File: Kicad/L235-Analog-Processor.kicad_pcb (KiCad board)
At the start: 2 copper layers, 190 x 125 mm, 295 parts, among them IC2 AD633ARZ-RL, J1 Input A, J10 Half Wave A + -B, J11 Inverted Out B, J12 CV Select, J13 CV Select, J15 Inverted Out A, J16 Full-Wave Rectifier A, J17 Half-Wave Rectifier A, J18 √(A²+B²), J2 Input B, J3 Function IN, J4 ( 10A / |B| ) / ( A * B / 10 ), J5 Output F(x), J6 Power, J7 Full-Wave Rectifier B, J8 A - B, J9 Negative Half-Wave Rectifier B, U1 TL082, U10 TL082, U11 TL082, U12 TL082, U13 TL084, U15 TL082, U16 RC4580, U17 TL082, U18 LM4040DBZ-10, U19 74HC148, U2 TL082, U20 LM339, U21 LM339, U22 74LS151, U23 74LS151, U24 74LS151, U25 74LS151, U26 74LS151, U27 74LS151, U28 74LS151, U29 LM339, U3 TL082, U30 LM339, U31 74HC148, U32 74LS151, U33 74LS151, U34 74LS151, U35 74LS151, U36 LM78M05_TO252, U4 TL082, U5 TL082, U6 TL082, U7 TL082, U8 TL082, U9 TL082

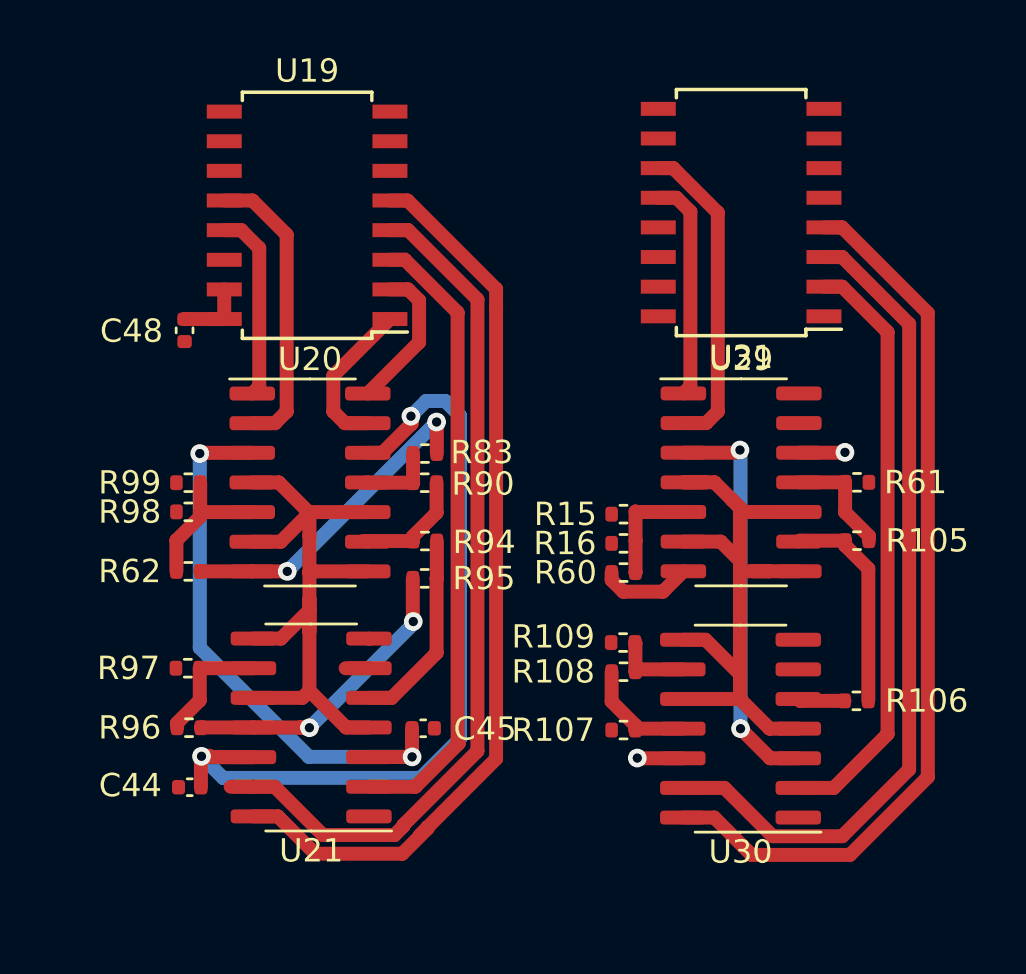
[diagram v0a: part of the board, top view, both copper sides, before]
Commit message: Added example of 3-bit flash adc and explained choice AD633
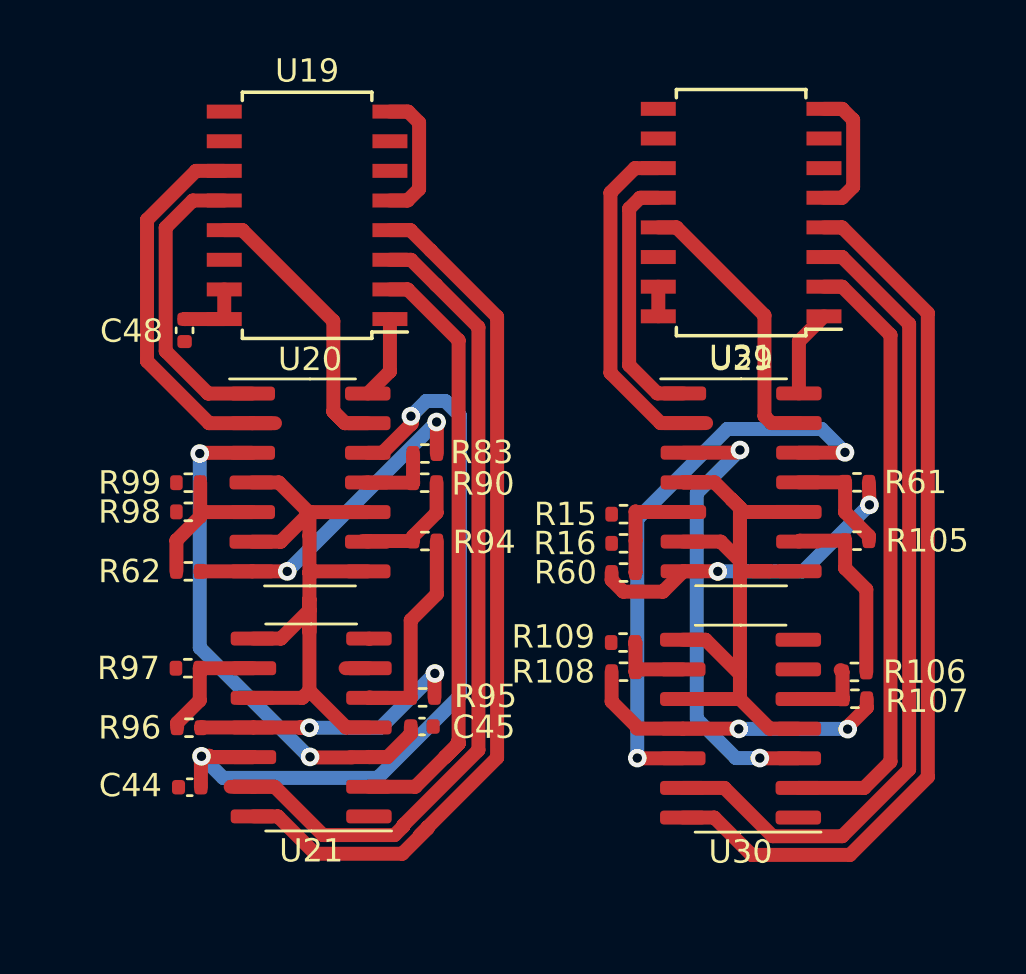
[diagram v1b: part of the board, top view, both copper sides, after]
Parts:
- moved R107 10.0 mm to (436.9, 3.66)
- moved R95 5.10 mm to (418.4, 3.60), turned to 180 degrees
- moved R106 1.24 mm to (436.9, 2.51)
- moved C45 0.09 mm to (418.4, 4.85)
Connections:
- U19 pad 1: Net-(U19-I4) -> Net-(U19-4)
- U19 pad 10: GND -> unconnected-(U19-0-Pad10)
- U19 pad 11: unconnected-(U19-I1-Pad11) -> Net-(U19-1)
- U19 pad 12: Net-(U19-I2) -> Net-(U19-2)
- U19 pad 13: Net-(U19-I3) -> Net-(U19-3)
- U19 pad 2: Net-(U19-I5) -> Net-(U19-5)
- U19 pad 3: Net-(U19-I6) -> Net-(U19-6)
- U19 pad 4: Net-(U19-I7) -> Net-(U19-7)
- U19 pad 5: Net-(U19-EI) -> GND
- U20 pad 1: Net-(U19-I3) -> Net-(U19-2)
- U20 pad 13: Net-(U19-I4) -> Net-(U19-3)
- U20 pad 14: Net-(U19-I5) -> Net-(U19-4)
- U20 pad 2: Net-(U19-I2) -> Net-(U19-1)
- U21 pad 13: Net-(U19-I7) -> Net-(U19-6)
- U21 pad 14: Net-(U19-EI) -> Net-(U19-7)
- U21 pad 2: Net-(U19-I6) -> Net-(U19-5)
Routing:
- net Net-(U19-EI): track 39.5 -> 0.00 mm
- net Net-(U19-7): track 0.00 -> 38.3 mm
- net Net-(U19-I7): track 37.3 -> 0.00 mm
- net Net-(U19-6): track 0.00 -> 36.1 mm
- net Net-(U19-I6): track 26.9 -> 0.00 mm
- net Net-(U19-5): track 0.00 -> 26.6 mm
- net -12V: track 105.0 -> 125.1 mm
- net Net-(U19-1): track 0.00 -> 16.8 mm
- net Net-(U19-2): track 0.00 -> 12.7 mm
- net Net-(U19-3): track 0.00 -> 12.6 mm
- net Net-(U19-I2): track 12.5 -> 0.00 mm
- net Net-(U31-3): track 0.00 -> 12.0 mm
- net GND: track 19.1 -> 30.7 mm
- net Net-(U29B-+): track 3.96 -> 14.4 mm, vias 0 -> 2
- net Net-(U30C-+): track 4.98 -> 13.9 mm, vias 0 -> 2
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
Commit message: Added header and mounting points
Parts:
- added ?: , , F.Cu at (374.0, 105.5)
- added H1: MountingHole, MountingHole:MountingHole_3.2mm_M3_DIN965, F.Cu at (374.0, 3.50)
- added H1: MountingHole, MountingHole:MountingHole_3.2mm_M3_DIN965, F.Cu at (319.0, 3.50)
- added H2: MountingHole, MountingHole:MountingHole_3.2mm_M3_DIN965, F.Cu at (393.0, 3.50)
- added H2: MountingHole, MountingHole:MountingHole_3.2mm_M3_DIN965, F.Cu at (338.0, 3.50)
- added H3: MountingHole, MountingHole:MountingHole_3.2mm_M3_DIN965, F.Cu at (319.0, 105.5)
- added H3: MountingHole, MountingHole:MountingHole_3.2mm_M3_DIN965, F.Cu at (374.0, 105.5)
- added J14: Conn_01x12_Pin, Connector_PinHeader_2.54mm:PinHeader_1x18_P2.54mm_Vertical, F.Cu at (338.0, 31.6)
- added J19: Conn_01x12_Socket, Connector_PinHeader_2.54mm:PinHeader_1x18_P2.54mm_Vertical, F.Cu at (393.0, 31.6)
- C10: value 0.01uF -> 10nF; footprint Capacitor_THT:C_Rect_L7.0mm_W2.5mm_P5.00mm -> Capacitor_SMD:C_0402_1005Metric
- C38, C39, D27, D28, RV1, RV2, RV3, RV4, RV5, RV6: moved to B.Cu
- C9: value 0.001uF -> 1nF; footprint Capacitor_THT:C_Rect_L7.0mm_W2.5mm_P5.00mm -> Capacitor_SMD:C_0402_1005Metric
- D24: footprint Diode_SMD:D_0402_1005Metric -> LED_THT:LED_D3.0mm_Clear
- J6: footprint Custom_Footprints:Eurorack_16_pin_header -> Custom_Footprints:Eurorack_10_pin_header; moved to B.Cu
- RV7, RV8: footprint Potentiometer_THT:Potentiometer_Alps_RK163_Single_Horizontal -> Potentiometer_THT:Potentiometer_Alpha_RD901F-40-00D_Single_Vertical
- moved C73 405.7 mm to (406.9, 52.0), turned to 180 degrees
- moved C72 397.9 mm to (398.7, 57.2), turned to -90 degrees
- moved R12 375.7 mm to (389.5, 35.8)
- moved R11 373.5 mm to (387.5, 35.3), turned to -90 degrees
- moved R14 372.9 mm to (386.8, 45.1)
- moved R10 371.3 mm to (385.6, 35.8), turned to 180 degrees
- moved R9 371.2 mm to (385.6, 34.8)
- moved R13 370.7 mm to (384.8, 45.1)
- moved C81 319.5 mm to (375.8, 37.4), turned to -90 degrees
- moved C82 315.7 mm to (374.5, 48.2), turned to 90 degrees
- moved IC2 302.1 mm to (375.2, 43.5), turned to -90 degrees
- moved U16 298.0 mm to (372.5, 34.5), turned to 90 degrees
- moved R59 297.4 mm to (339.2, 107.0), turned to -90 degrees
- moved R73 288.0 mm to (337.5, 102.8), turned to 180 degrees
- moved R70 287.7 mm to (337.5, 89.0)
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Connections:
- R91 pad 2: * OUT -> AD534_OUT
- U22 pad 12: B_IN_BUFFERED -> B
- U22 pad 15: A_IN_BUFFERED -> A
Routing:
- net -12V: track 125.1 -> 456.5 mm, vias 8 -> 24
- net +12V: track 85.7 -> 406.2 mm, vias 7 -> 21
- net +5V: track 4.24 -> 133.6 mm, vias 0 -> 3
- net A: track 127.3 -> 254.5 mm, vias 0 -> 6
- net GND: track 30.7 -> 137.8 mm, vias 11 -> 20
- net <X>: track 0.00 -> 105.7 mm, vias 0 -> 1
- net B0: track 0.00 -> 105.1 mm, vias 0 -> 5
- net Net-(U7B--): track 0.00 -> 96.0 mm
- net A1: track 0.00 -> 79.3 mm, vias 0 -> 5
- net A2: track 0.00 -> 77.0 mm, vias 0 -> 5
- net AD534_OUT: track 0.00 -> 72.3 mm, vias 0 -> 6
- net A0: track 0.00 -> 71.3 mm, vias 0 -> 6
- net B: track 106.0 -> 176.8 mm, vias 0 -> 2
- net B2: track 0.00 -> 54.0 mm, vias 0 -> 4
- net Net-(J18-PadT): track 0.00 -> 53.2 mm, vias 0 -> 1
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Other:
- board size 190 x 125 mm -> 110 x 110 mm
- board text added: "Input A"
- board text added: "Input B"

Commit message: Optimized PCB routing, started with variable resistor
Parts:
- removed ?: , 
- removed U16: RC4580, Package_SO:SOIC-8_3.9x4.9mm_P1.27mm
- added U14: RC4580, Package_SO:SOIC-8_3.9x4.9mm_P1.27mm, F.Cu at (380.8, 35.9)
- added U37: TL082, Package_SO:SOIC-8_3.9x4.9mm_P1.27mm, F.Cu at (404.7, 25.3)
- C25: footprint Capacitor_THT:C_Rect_L7.0mm_W2.5mm_P5.00mm -> Capacitor_SMD:C_0402_1005Metric
- U22, U23, U24, U25, U26, U28, U32, U33, U34, U35: value 74LS151 -> DG4051E
- moved R33 268.2 mm to (411.1, 5.21), turned to 90 degrees
- moved RV3 263.7 mm to (406.3, 3.10), turned to -90 degrees
- moved C70 262.0 mm to (383.9, 80.2), turned to 180 degrees
- moved R27 259.4 mm to (410.5, 26.4), turned to -90 degrees
- moved R22 257.8 mm to (409.5, 14.0), turned to 90 degrees
- moved R31 256.1 mm to (402.3, 11.9)
- moved R23 253.3 mm to (404.5, 11.9), turned to 180 degrees
- moved R25 253.1 mm to (404.5, 21.9)
- moved R26 252.5 mm to (403.4, 20.6)
- moved R28 252.4 mm to (400.2, 8.14), turned to 90 degrees
- moved R29 251.7 mm to (401.0, 20.6), turned to 180 degrees
- moved R30 251.5 mm to (398.8, 13.4)
- moved R32 251.3 mm to (398.9, 23.1)
- moved R24 249.2 mm to (400.5, 16.6), turned to -90 degrees
- moved R21 248.8 mm to (401.1, 32.1)
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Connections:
- C25 pad 1: Net-(U11A--) -> Net-(U37A--)
- J14 pad 16: √(A²+B²) -> GND
- J14 pad 2: A -> X
- J14 pad 4: B -> √(A²+B²)
- J14 pad 6: X -> A
- J14 pad 8: GND -> -12V
- J14 pad 9: -12V -> B
- J15 pad G: GND -> unconnected-(J15-PadG)
- J19 pad 16: √(A²+B²) -> GND
- J19 pad 2: A -> X
- J19 pad 4: B -> √(A²+B²)
- J19 pad 6: X -> A
- J19 pad 8: GND -> -12V
- J19 pad 9: -12V -> B
- R25 pad 1: Net-(U13A-+) -> Net-(U37B--)
- R26 pad 2: Net-(U13A-+) -> Net-(U37B--)
- R27 pad 1: Net-(U11A--) -> Net-(U37A--)
- R30 pad 1: Net-(U13A--) -> Net-(U37B-+)
- R33 pad 2: Net-(U6A-+) -> Net-(R33-Pad2)
- RV3 pad 1: Net-(U6A-+) -> Net-(R33-Pad2)
- TR1 pad 4: Net-(U11A--) -> Net-(U37A--)
- TR1 pad 6: Net-(U11A--) -> Net-(U37A--)
- TR2 pad 4: Net-(U6A-+) -> Net-(R33-Pad2)
- TR2 pad 5: Net-(U13A--) -> Net-(U37B-+)
- U11 pad 1: √(A²+B²) -> (-dX/dt) or (-dX/dt*1/100)
- U11 pad 2: Net-(U11A--) -> F1
- U13 pad 1: Net-(U13A--) -> (no net)
- U13 pad 2: Net-(U13A--) -> (no net)
- U13 pad 3: Net-(U13A-+) -> (no net)
- U7 pad 1: (-dX/dt) or (-dX/dt*1/100) -> Net-(U7A-+)
- U7 pad 2: F1 -> GND
- U7 pad 3: GND -> Net-(U7A-+)
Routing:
- net 10V REF: track 42.5 -> 270.5 mm, vias 0 -> 3
- net -12V: track 456.5 -> 641.3 mm, vias 24 -> 35
- net +12V: track 406.2 -> 565.4 mm, vias 21 -> 28
- net GND: track 137.8 -> 291.9 mm, vias 20 -> 57
- net Net-(U14C-V+): track 19.8 -> 103.1 mm, vias 2 -> 5
- net <X>: track 105.7 -> 187.0 mm, vias 1 -> 0
- net √(A²+B²): track 11.6 -> 78.2 mm, vias 0 -> 1
- net B0: track 105.1 -> 43.0 mm, vias 5 -> 4
- net |B|: track 42.5 -> 104.5 mm, vias 2 -> 1
- net F1: track 0.00 -> 57.9 mm, vias 0 -> 1
- net B: track 176.8 -> 234.6 mm, vias 2 -> 1
- net AD534_OUT: track 72.3 -> 129.6 mm, vias 6 -> 5
- net X²: track 0.00 -> 56.6 mm, vias 0 -> 3
- net Net-(D10-A): track 0.00 -> 50.3 mm, vias 0 -> 2
- net A - B: track 22.7 -> 71.4 mm
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
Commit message: All components routed
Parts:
- removed C17, C18, C79: 100nF, Capacitor_SMD:C_0402_1005Metric
- removed D27, D28: 1N5819, Diode_SMD:D_0402_1005Metric
- removed IC2: AD633ARZ-RL, Package_SO:SOIC-8_3.9x4.9mm_P1.27mm
- added D33: 1N5819HW, Diode_SMD:D_SOD-123, F.Cu at (399.8, 61.7)
- added D34: 1N5819HW, Diode_SMD:D_SOD-123, F.Cu at (399.9, 51.2)
- added U16: AD633ARZ-RL, Package_SO:SOIC-8_3.9x4.9mm_P1.27mm, F.Cu at (380.7, 50.2)
- J14: value Conn_01x12_Pin -> Conn_01x20_Pin; footprint Connector_PinHeader_2.54mm:PinHeader_1x18_P2.54mm_Vertical -> Connector_PinHeader_2.54mm:PinHeader_1x20_P2.54mm_Vertical
- J19: value Conn_01x12_Socket -> Conn_01x20_Socket; footprint Connector_PinHeader_2.54mm:PinHeader_1x18_P2.54mm_Vertical -> Connector_PinHeader_2.54mm:PinHeader_1x20_P2.54mm_Vertical
- moved C22 185.6 mm to (407.3, 5.28), turned to 180 degrees
- moved C20 176.0 mm to (407.9, 12.1), turned to 180 degrees
- moved C21 173.7 mm to (399.8, 10.5), turned to 180 degrees
- moved C80 172.4 mm to (384.5, 32.6)
- moved C19 165.6 mm to (403.3, 18.7), turned to 180 degrees
- moved C78 156.7 mm to (376.3, 38.3), turned to 90 degrees
- moved C76 148.7 mm to (408.2, 104.0)
- moved C75 142.7 mm to (408.3, 87.0), turned to 180 degrees
- moved C77 138.8 mm to (398.9, 104.5), turned to 90 degrees
- moved C74 137.7 mm to (398.4, 90.8), turned to 180 degrees
- moved C56 135.5 mm to (400.3, 86.7), turned to 180 degrees
- moved C58 133.6 mm to (389.4, 87.1), turned to -90 degrees
- moved C59 126.6 mm to (380.7, 89.8)
- moved C60 113.4 mm to (376.1, 80.0)
- moved C46 111.8 mm to (388.8, 19.6), turned to 180 degrees
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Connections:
- C74 pad 1: Net-(U14C-V+) -> +12V
- C76 pad 1: Net-(U14C-V+) -> +12V
- C80 pad 1: Net-(U14C-V+) -> +12V
- J14 pad 1: CV_SELECT -> unconnected-(J14-Pin_1-Pad1)
- J14 pad 10: Function Out -> -12V
- J14 pad 11: <X> -> B
- J14 pad 12: 10V REF -> Function Out
- J14 pad 13: GND -> <X>
- J14 pad 14: A - B -> 10V REF
- J14 pad 15: AD534_OUT -> GND
- J14 pad 16: GND -> A - B
- J14 pad 17: GND -> AD534_OUT
- J14 pad 18: CV_FUNCTION -> GND
- J14 pad 2: X -> GND
- J14 pad 3: |A| -> CV_SELECT
- J14 pad 4: √(A²+B²) -> X
- J14 pad 5: |B| -> |A|
- J14 pad 6: A -> √(A²+B²)
- J14 pad 7: +12V -> |B|
- J14 pad 8: -12V -> A
- J14 pad 9: B -> +12V
- J19 pad 1: CV_SELECT -> unconnected-(J19-Pin_1-Pad1)
- J19 pad 10: Function Out -> -12V
- J19 pad 11: <X> -> B
- J19 pad 12: 10V REF -> Function Out
- J19 pad 13: GND -> <X>
- J19 pad 14: A - B -> 10V REF
- J19 pad 15: AD534_OUT -> GND
- J19 pad 16: GND -> A - B
- J19 pad 17: GND -> AD534_OUT
- J19 pad 18: CV_FUNCTION -> GND
- J19 pad 2: X -> GND
- J19 pad 3: |A| -> CV_SELECT
- J19 pad 4: √(A²+B²) -> X
- J19 pad 5: |B| -> |A|
- J19 pad 6: A -> √(A²+B²)
- J19 pad 7: +12V -> |B|
- J19 pad 8: -12V -> A
- J19 pad 9: B -> +12V
- U13 pad 1: (no net) -> Net-(U13A-+)
- U13 pad 2: (no net) -> GND
- U13 pad 3: (no net) -> Net-(U13A-+)
- U14 pad 8: Net-(U14C-V+) -> +12V
- U29 pad 3: Net-(U14C-V+) -> +12V
- U30 pad 3: Net-(U14C-V+) -> +12V
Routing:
- net GND: track 291.9 -> 411.6 mm, vias 57 -> 83
- net |A|: track 38.7 -> 148.0 mm, vias 2 -> 4
- net X: track 45.5 -> 153.0 mm, vias 0 -> 2
- net Net-(U14C-V+): track 103.1 -> 0.00 mm, vias 5 -> 0
- net +12V: track 565.4 -> 663.8 mm, vias 28 -> 33
- net |B|: track 104.5 -> 191.7 mm, vias 1 -> 3
- net Function Out: track 35.5 -> 91.3 mm
- net -12V: track 641.3 -> 670.4 mm, vias 35 -> 34
- net A: track 273.8 -> 296.0 mm, vias 5 -> 7
- net Net-(D19-K): track 12.9 -> 34.7 mm
- net √|x| or X²: track 10.1 -> 26.6 mm, vias 0 -> 2
- net Net-(U13B--): track 39.7 -> 26.9 mm
- net Net-(J4-PadT): track 34.6 -> 23.0 mm
- net Net-(U7B--): track 96.0 -> 86.8 mm
- net B: track 234.6 -> 226.5 mm
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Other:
- board text added: "Version 1.0 Lytrix 2024"
